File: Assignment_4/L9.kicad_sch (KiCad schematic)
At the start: 31 parts, among them J1 USB_B, J2 Conn_01x06_Socket, J3 Conn_01x05_Socket, J4 Jack-DC, J5 Conn_01x02_Socket, J6 Conn_01x08_Socket, J7 Conn_01x08_Socket, J8 Conn_01x08_Socket, J9 Conn_01x08_Socket, SW1 SW_Push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

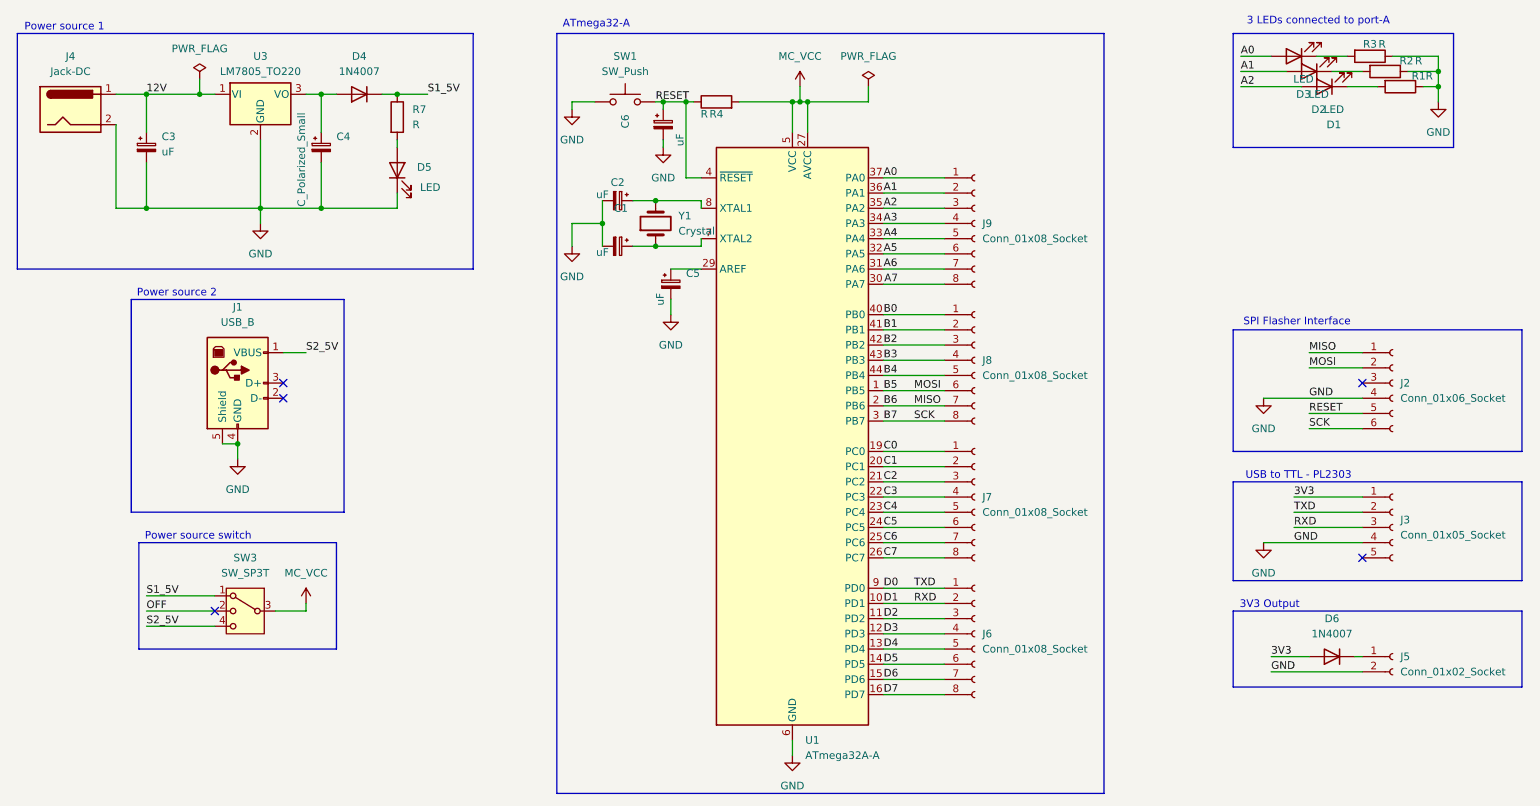
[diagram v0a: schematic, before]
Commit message: Add custom components for all assignments
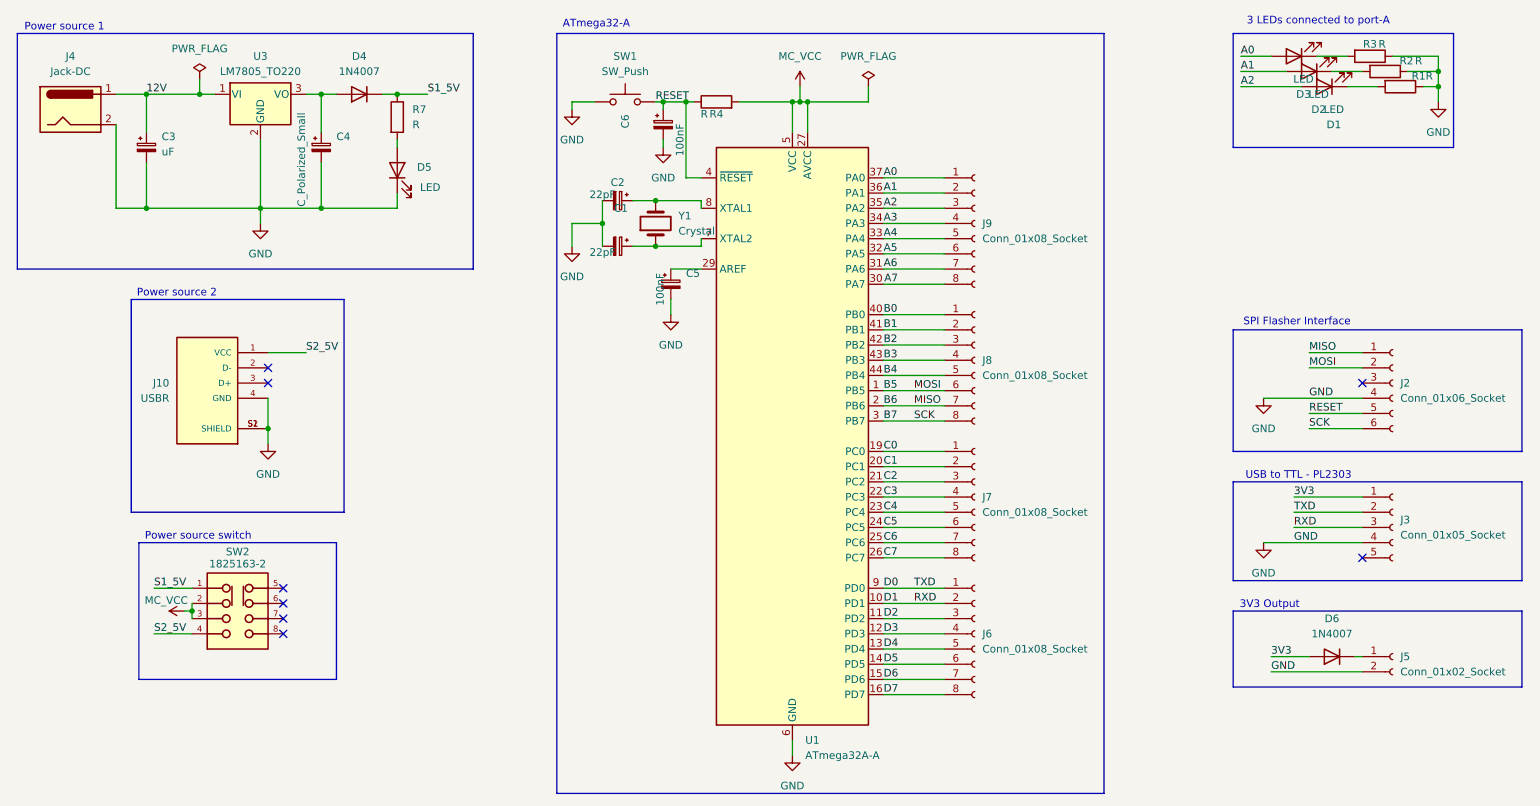
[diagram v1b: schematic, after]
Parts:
- removed J1: USB_B, Connector_USB:USB_B_TE_5787834_Vertical, symbol Connector:USB_B
- removed SW3: SW_SP3T, symbol Switch:SW_SP3T
- added J10: USBR, Usb-B:SAMTEC_USBR-B-S-S-O-TH, symbol USBR-B-S-S-O-TH:USBR-B-S-S-O-TH
- added SW2: 1825163-2, DP3T:SW_1825163-2, symbol 1825163-2:1825163-2
- C1, C2: value uF -> 22pF; footprint (none) -> Capacitor_THT:C_Disc_D5.1mm_W3.2mm_P5.00mm
- C5, C6: value uF -> 100nF; footprint (none) -> Capacitor_THT:C_Disc_D3.0mm_W2.0mm_P2.50mm
- D1, D2, D3: footprint (none) -> LED_THT:LED_D5.0mm
- J3: footprint (none) -> Connector_PinHeader_2.54mm:PinHeader_1x05_P2.54mm_Horizontal
- J4: footprint (none) -> Connector_BarrelJack:BarrelJack_Horizontal
- J5: footprint (none) -> Connector_PinHeader_2.54mm:PinHeader_1x02_P2.54mm_Vertical
- J6, J7, J8, J9: footprint (none) -> Connector_PinSocket_2.54mm:PinSocket_1x08_P2.54mm_Vertical
- R1, R2, R3, R4: footprint (none) -> Resistor_THT:R_Axial_DIN0204_L3.6mm_D1.6mm_P5.08mm_Horizontal
- SW1: footprint (none) -> Button_Switch_THT:SW_PUSH_6mm_H5mm
- Y1: footprint (none) -> Crystal:Crystal_HC49-4H_Vertical
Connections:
- net GND: now also J10.4 (GND), J10.S1 (SHIELD), J10.S2 (SHIELD)
- net MC_VCC: now also SW2.2, SW2.3
- net S1_5V: now also SW2.1
- net S2_5V: now also J10.1 (VCC), SW2.4
- no-connect marks 5 -> 8

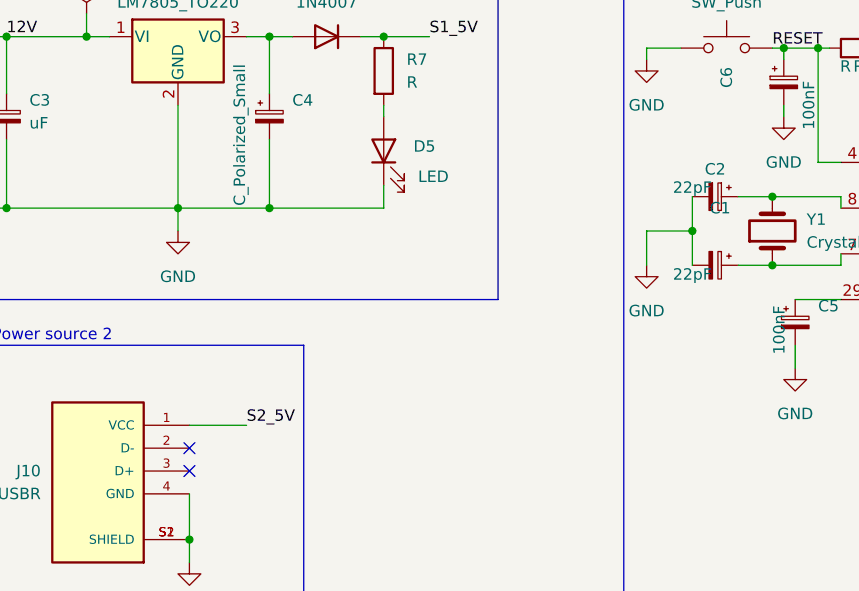
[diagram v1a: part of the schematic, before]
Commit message: Assignment_4: Add layout P1
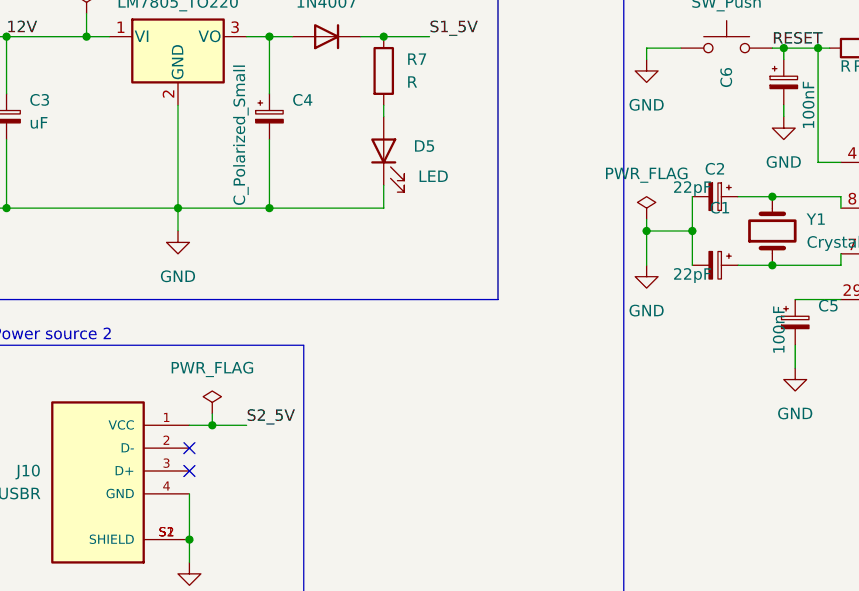
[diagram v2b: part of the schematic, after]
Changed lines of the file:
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@@
 	)
 	(junction
+		(at 118.11 63.5)
+		(diameter 0)
+		(color 0 0 0 0)
+	)
+	(junction
 		(at 123.19 63.5)
 		(diameter 0)
@@
 		(color 0 0 0 0)
 	)
+	(junction
+		(at 69.85 85.09)
+		(diameter 0)
+		(color 0 0 0 0)
+	)
 	(no_connect
 		(at 69.85 124.46)
@@
 	(wire
 		(pts
+			(xy 118.11 62.23) (xy 118.11 63.5)
+		)
+		(stroke
+			(width 0)
+			(type default)
+		)
+	)
+	(wire
+		(pts
 			(xy 88.9 60.96) (xy 76.2 60.96)
 		)
@@
 	(wire
 		(pts
+			(xy 69.85 85.09) (xy 67.31 85.09)
+		)
+		(stroke
+			(width 0)
+			(type default)
+		)
+	)
+	(wire
+		(pts
 			(xy 170.18 91.44) (xy 180.34 91.44)
 		)
@@
 	(wire
 		(pts
-			(xy 73.66 85.09) (xy 67.31 85.09)
+			(xy 73.66 85.09) (xy 69.85 85.09)
 		)
 		(stroke
@@
 	(wire
 		(pts
+			(xy 69.85 83.82) (xy 69.85 85.09)
+		)
+		(stroke
+			(width 0)
+			(type default)
+		)
+	)
+	(wire
+		(pts
 			(xy 229.87 35.56) (xy 234.95 35.56)
 		)
@@
 	(symbol
 		(lib_id "power:PWR_FLAG")
+		(at 118.11 62.23 0)
+		(unit 1)
+		(exclude_from_sim no)
+		(in_bom yes)
+		(on_board yes)
+		(dnp no)
+		(fields_autoplaced yes)
+		(property "Reference" "#FLG06"
+			(at 118.11 60.325 0)
+			(effects
+				(font
+					(size 1.27 1.27)
+				)
+				(hide yes)
+			)
+		)
+		(property "Value" "PWR_FLAG"
+			(at 118.11 57.15 0)
+			(effects
+				(font
+					(size 1.27 1.27)
+				)
+			)
+		)
+		(property "Footprint" ""
+			(at 118.11 62.23 0)
+			(effects
+				(font
+					(size 1.27 1.27)
+				)
+				(hide yes)
+			)
+		)
+		(property "Datasheet" "~"
+			(at 118.11 62.23 0)
+			(effects
+				(font
+					(size 1.27 1.27)
+				)
+				(hide yes)
+			)
+		)
+		(property "Description" "Special symbol for telling ERC where power comes from"
+			(at 118.11 62.23 0)
+			(effects
+				(font
+					(size 1.27 1.27)
+				)
+				(hide yes)
+			)
+		)
+		(pin "1"
+		)
+		(instances
+			(project "L9"
+				(path "/3c8dddeb-1dc8-43d1-89c8-2e8251a5c7a9"
+					(reference "#FLG06")
+					(unit 1)
+				)
+			)
+		)
+	)
+	(symbol
+		(lib_id "power:PWR_FLAG")
 		(at 167.64 40.64 0)
 		(unit 1)
@@
 					(unit 1)
 				)
+			)
+		)
+	)
+	(symbol
+		(lib_id "power:PWR_FLAG")
+		(at 69.85 83.82 0)
+		(unit 1)
+		(exclude_from_sim no)
+		(in_bom yes)
+		(on_board yes)
+		(dnp no)
+		(fields_autoplaced yes)
+		(property "Reference" "#FLG05"
+			(at 69.85 81.915 0)
+			(effects
+				(font
+					(size 1.27 1.27)
+				)
+				(hide yes)
+			)
+		)
+		(property "Value" "PWR_FLAG"
+			(at 69.85 78.74 0)
+			(effects
+				(font
+					(size 1.27 1.27)
+				)
+			)
+		)
+		(property "Footprint" ""
+			(at 69.85 83.82 0)
+			(effects
+				(font
+					(size 1.27 1.27)
+				)
+				(hide yes)
+			)
+		)
+		(property "Datasheet" "~"
+			(at 69.85 83.82 0)
+			(effects
+				(font
+					(size 1.27 1.27)
+				)
+				(hide yes)
+			)
+		)
+		(property "Description" "Special symbol for telling ERC where power comes from"
+			(at 69.85 83.82 0)
+			(effects
+				(font
+					(size 1.27 1.27)
+				)
+				(hide yes)
+			)
+		)
+		(pin "1"
+		)
+		(instances
+			(project "L9"
+				(path "/3c8dddeb-1dc8-43d1-89c8-2e8251a5c7a9"
+					(reference "#FLG05")
+					(unit 1)
+				)
